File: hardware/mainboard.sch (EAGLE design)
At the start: 38 parts, among them IC1 24LC512P

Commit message: extio.brd, mainboard.brd, gate433.lib
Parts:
- R1, R2, R3, R4, R5, R6, R7, R8: device resistor:R-EU_0204_7 -> resistor:R-EU_R0603
- renumbered IOEXT1 to EXTIO1

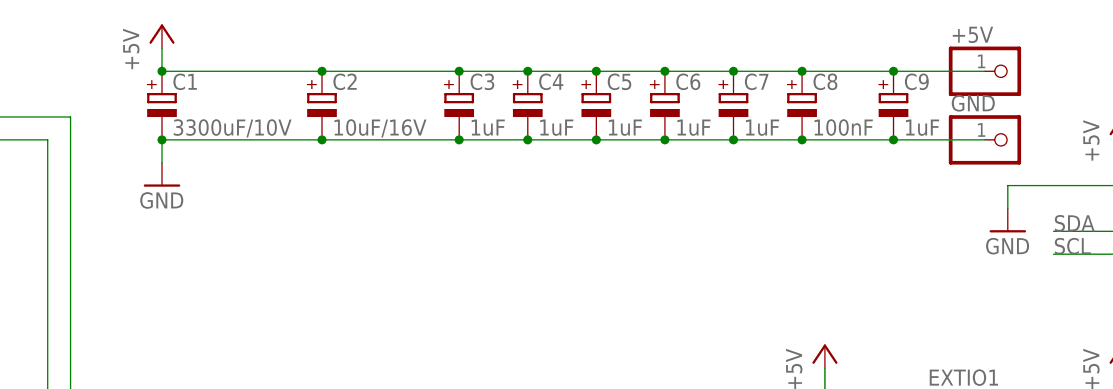
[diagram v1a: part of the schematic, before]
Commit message: mainboard SMD update
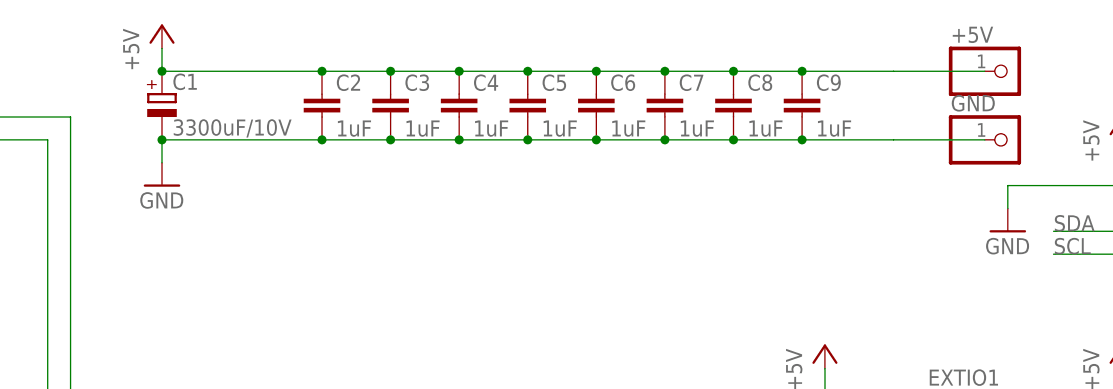
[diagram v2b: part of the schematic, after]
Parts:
- C2: value 10uF/16V -> 1uF; device resistor:CPOL-EUTT2D4 -> resistor:C-EUC0603
- C3, C4, C5, C6, C7, C9: device resistor:CPOL-EUTT2D4 -> resistor:C-EUC0603
- C8: value 100nF -> 1uF; device resistor:CPOL-EUTT2D4 -> resistor:C-EUC0603
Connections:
- net +5V: now also C2.1, C3.1, C4.1, C5.1, C6.1, C7.1, C8.1, C9.1; no longer C2.+, C3.+, C4.+, C5.+, C6.+, C7.+, C8.+, C9.+
- net GND: now also C2.2, C3.2, C4.2, C5.2, C6.2, C7.2, C8.2, C9.2; no longer C2.-, C3.-, C4.-, C5.-, C6.-, C7.-, C8.-, C9.-
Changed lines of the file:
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@@
 <part name="P+12" library="supply1" deviceset="+5V" device=""/>
 <part name="GND14" library="supply1" deviceset="GND" device=""/>
-<part name="C2" library="resistor" deviceset="CPOL-EU" device="TT2D4" value="10uF/16V"/>
-<part name="C3" library="resistor" deviceset="CPOL-EU" device="TT2D4" value="1uF"/>
-<part name="C4" library="resistor" deviceset="CPOL-EU" device="TT2D4" value="1uF"/>
-<part name="C5" library="resistor" deviceset="CPOL-EU" device="TT2D4" value="1uF"/>
-<part name="C6" library="resistor" deviceset="CPOL-EU" device="TT2D4" value="1uF"/>
+<part name="C3" library="resistor" deviceset="C-EU" device="C0603" value="1uF"/>
+<part name="C4" library="resistor" deviceset="C-EU" device="C0603" value="1uF"/>
+<part name="C5" library="resistor" deviceset="C-EU" device="C0603" value="1uF"/>
+<part name="C6" library="resistor" deviceset="C-EU" device="C0603" value="1uF"/>
 <part name="OK3" library="gate433" deviceset="PC817" device=""/>
 <part name="OK4" library="gate433" deviceset="PC817" device=""/>
@@
 <part name="+3V2" library="supply1" deviceset="+3V3" device=""/>
 <part name="JP5" library="gate433" deviceset="JP1E" device=""/>
-<part name="C7" library="resistor" deviceset="CPOL-EU" device="TT2D4" value="1uF"/>
-<part name="C8" library="resistor" deviceset="CPOL-EU" device="TT2D4" value="100nF"/>
-<part name="C9" library="resistor" deviceset="CPOL-EU" device="TT2D4" value="1uF"/>
+<part name="C7" library="resistor" deviceset="C-EU" device="C0603" value="1uF"/>
+<part name="C2" library="resistor" deviceset="C-EU" device="C0603" value="1uF"/>
 <part name="JP1" library="gate433" deviceset="PINHD-1X9" device=""/>
 <part name="JP2" library="gate433" deviceset="PINHD-2X6" device=""/>
@@
 <part name="GND16" library="supply1" deviceset="GND" device=""/>
 <part name="P+17" library="supply1" deviceset="+5V" device=""/>
+<part name="C8" library="resistor" deviceset="C-EU" device="C0603" value="1uF"/>
+<part name="C9" library="resistor" deviceset="C-EU" device="C0603" value="1uF"/>
 </parts>
 <sheets>
@@
 <instance part="P+12" gate="1" x="101.6" y="172.72"/>
 <instance part="GND14" gate="1" x="101.6" y="154.94"/>
-<instance part="C2" gate="G$1" x="119.38" y="165.1"/>
-<instance part="C3" gate="G$1" x="134.62" y="165.1"/>
-<instance part="C4" gate="G$1" x="142.24" y="165.1"/>
-<instance part="C5" gate="G$1" x="149.86" y="165.1"/>
-<instance part="C6" gate="G$1" x="157.48" y="165.1"/>
+<instance part="C3" gate="G$1" x="127" y="165.1"/>
+<instance part="C4" gate="G$1" x="134.62" y="165.1"/>
+<instance part="C5" gate="G$1" x="142.24" y="165.1"/>
+<instance part="C6" gate="G$1" x="149.86" y="165.1"/>
 <instance part="OK3" gate="A" x="73.66" y="66.04"/>
 <instance part="OK4" gate="A" x="73.66" y="50.8"/>
@@
 <instance part="+3V2" gate="G$1" x="50.8" y="139.7"/>
 <instance part="JP5" gate="A" x="40.64" y="132.08" rot="MR0"/>
-<instance part="C7" gate="G$1" x="165.1" y="165.1"/>
-<instance part="C8" gate="G$1" x="172.72" y="165.1"/>
-<instance part="C9" gate="G$1" x="182.88" y="165.1"/>
+<instance part="C7" gate="G$1" x="157.48" y="165.1"/>
+<instance part="C2" gate="G$1" x="119.38" y="165.1"/>
 <instance part="JP1" gate="A" x="10.16" y="119.38" rot="MR0"/>
 <instance part="JP2" gate="A" x="30.48" y="88.9" rot="MR0"/>
@@
 <instance part="GND16" gate="1" x="167.64" y="124.46"/>
 <instance part="P+17" gate="1" x="175.26" y="137.16"/>
+<instance part="C8" gate="G$1" x="165.1" y="165.1"/>
+<instance part="C9" gate="G$1" x="172.72" y="165.1"/>
 </instances>
 <busses>
@@
 <pinref part="P+12" gate="1" pin="+5V"/>
 <wire x1="101.6" y1="170.18" x2="101.6" y2="167.64" width="0.1524" layer="91"/>
-<pinref part="C6" gate="G$1" pin="+"/>
-<pinref part="C5" gate="G$1" pin="+"/>
-<wire x1="157.48" y1="167.64" x2="149.86" y2="167.64" width="0.1524" layer="91"/>
-<pinref part="C4" gate="G$1" pin="+"/>
+<pinref part="C6" gate="G$1" pin="1"/>
+<pinref part="C5" gate="G$1" pin="1"/>
 <wire x1="149.86" y1="167.64" x2="142.24" y2="167.64" width="0.1524" layer="91"/>
-<junction x="149.86" y="167.64"/>
-<pinref part="C3" gate="G$1" pin="+"/>
+<pinref part="C4" gate="G$1" pin="1"/>
 <wire x1="142.24" y1="167.64" x2="134.62" y2="167.64" width="0.1524" layer="91"/>
 <junction x="142.24" y="167.64"/>
-<pinref part="C2" gate="G$1" pin="+"/>
-<wire x1="134.62" y1="167.64" x2="119.38" y2="167.64" width="0.1524" layer="91"/>
+<pinref part="C3" gate="G$1" pin="1"/>
+<wire x1="134.62" y1="167.64" x2="127" y2="167.64" width="0.1524" layer="91"/>
 <junction x="134.62" y="167.64"/>
-<wire x1="119.38" y1="167.64" x2="101.6" y2="167.64" width="0.1524" layer="91"/>
+<junction x="127" y="167.64"/>
+<junction x="101.6" y="167.64"/>
+<pinref part="C7" gate="G$1" pin="1"/>
+<wire x1="149.86" y1="167.64" x2="157.48" y2="167.64" width="0.1524" layer="91"/>
+<junction x="149.86" y="167.64"/>
+<pinref part="C2" gate="G$1" pin="1"/>
+<junction x="157.48" y="167.64"/>
 <junction x="119.38" y="167.64"/>
-<junction x="101.6" y="167.64"/>
-<pinref part="C7" gate="G$1" pin="+"/>
-<wire x1="157.48" y1="167.64" x2="165.1" y2="167.64" width="0.1524" layer="91"/>
-<junction x="157.48" y="167.64"/>
-<pinref part="C8" gate="G$1" pin="+"/>
-<wire x1="165.1" y1="167.64" x2="172.72" y2="167.64" width="0.1524" layer="91"/>
-<junction x="165.1" y="167.64"/>
-<pinref part="C9" gate="G$1" pin="+"/>
-<wire x1="172.72" y1="167.64" x2="182.88" y2="167.64" width="0.1524" layer="91"/>
-<junction x="172.72" y="167.64"/>
 <pinref part="+5V" gate="G$1" pin="1"/>
 <wire x1="182.88" y1="167.64" x2="193.04" y2="167.64" width="0.1524" layer="91"/>
-<junction x="182.88" y="167.64"/>
+<wire x1="101.6" y1="167.64" x2="119.38" y2="167.64" width="0.1524" layer="91"/>
+<wire x1="127" y1="167.64" x2="119.38" y2="167.64" width="0.1524" layer="91"/>
+<wire x1="182.88" y1="167.64" x2="172.72" y2="167.64" width="0.1524" layer="91"/>
+<pinref part="C8" gate="G$1" pin="1"/>
+<wire x1="172.72" y1="167.64" x2="165.1" y2="167.64" width="0.1524" layer="91"/>
+<wire x1="165.1" y1="167.64" x2="157.48" y2="167.64" width="0.1524" layer="91"/>
+<junction x="165.1" y="167.64"/>
+<pinref part="C9" gate="G$1" pin="1"/>
+<junction x="172.72" y="167.64"/>
 </segment>
 <segment>
@@
 <pinref part="GND14" gate="1" pin="GND"/>
 <wire x1="101.6" y1="157.48" x2="101.6" y2="160.02" width="0.1524" layer="91"/>
-<pinref part="C2" gate="G$1" pin="-"/>
-<wire x1="101.6" y1="160.02" x2="119.38" y2="160.02" width="0.1524" layer="91"/>
 <junction x="101.6" y="160.02"/>
-<pinref part="C3" gate="G$1" pin="-"/>
-<wire x1="119.38" y1="160.02" x2="134.62" y2="160.02" width="0.1524" layer="91"/>
-<junction x="119.38" y="160.02"/>
-<pinref part="C4" gate="G$1" pin="-"/>
+<pinref part="C3" gate="G$1" pin="2"/>
+<pinref part="C4" gate="G$1" pin="2"/>
+<wire x1="127" y1="160.02" x2="134.62" y2="160.02" width="0.1524" layer="91"/>
+<junction x="127" y="160.02"/>
+<pinref part="C5" gate="G$1" pin="2"/>
 <wire x1="134.62" y1="160.02" x2="142.24" y2="160.02" width="0.1524" layer="91"/>
 <junction x="134.62" y="160.02"/>
-<pinref part="C5" gate="G$1" pin="-"/>
+<pinref part="C6" gate="G$1" pin="2"/>
 <wire x1="142.24" y1="160.02" x2="149.86" y2="160.02" width="0.1524" layer="91"/>
 <junction x="142.24" y="160.02"/>
-<pinref part="C6" gate="G$1" pin="-"/>
-<wire x1="149.86" y1="160.02" x2="157.48" y2="160.02" width="0.1524" layer="91"/>
+<pinref part="C2" gate="G$1" pin="2"/>
+<pinref part="C7" gate="G$1" pin="2"/>
+<junction x="119.38" y="160.02"/>
+<wire x1="157.48" y1="160.02" x2="149.86" y2="160.02" width="0.1524" layer="91"/>
+<junction x="157.48" y="160.02"/>
 <junction x="149.86" y="160.02"/>
-<pinref part="C9" gate="G$1" pin="-"/>
-<pinref part="C8" gate="G$1" pin="-"/>
+<pinref part="GND" gate="G$1" pin="1"/>
+<wire x1="182.88" y1="160.02" x2="193.04" y2="160.02" width="0.1524" layer="91"/>
+<wire x1="101.6" y1="160.02" x2="119.38" y2="160.02" width="0.1524" layer="91"/>
+<wire x1="127" y1="160.02" x2="119.38" y2="160.02" width="0.1524" layer="91"/>
 <wire x1="182.88" y1="160.02" x2="172.72" y2="160.02" width="0.1524" layer="91"/>
-<pinref part="C7" gate="G$1" pin="-"/>
+<pinref part="C8" gate="G$1" pin="2"/>
 <wire x1="172.72" y1="160.02" x2="165.1" y2="160.02" width="0.1524" layer="91"/>
-<junction x="172.72" y="160.02"/>
 <wire x1="165.1" y1="160.02" x2="157.48" y2="160.02" width="0.1524" layer="91"/>
 <junction x="165.1" y="160.02"/>
-<junction x="157.48" y="160.02"/>
-<pinref part="GND" gate="G$1" pin="1"/>
-<wire x1="182.88" y1="160.02" x2="193.04" y2="160.02" width="0.1524" layer="91"/>
-<junction x="182.88" y="160.02"/>
-</segment>
-<segment>
+<pinref part="C9" gate="G$1" pin="2"/>
+<junction x="172.72" y="160.02"/>
+</segment>
+<segment>
